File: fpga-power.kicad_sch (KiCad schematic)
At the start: 107 parts, among them U34 XCAU25P-2FFVB676I

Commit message: [#68016] Clean-up the schematic
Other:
- moved on the sheet: R36

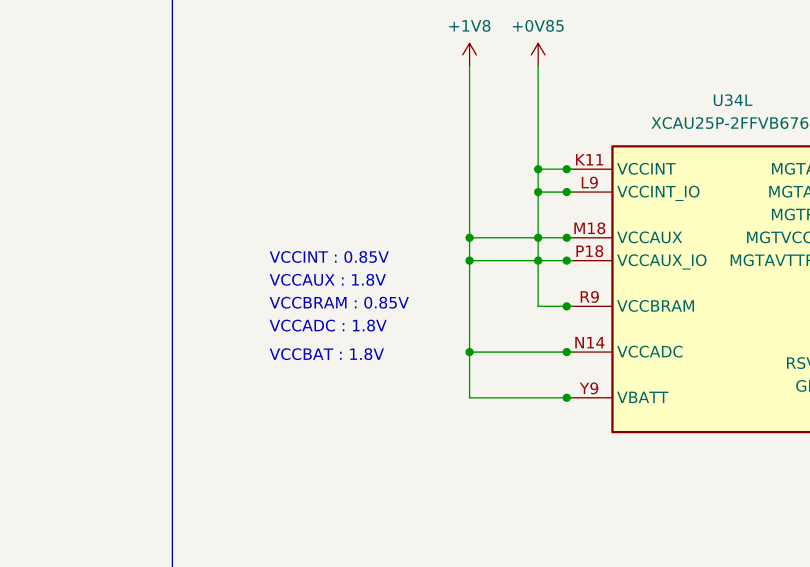
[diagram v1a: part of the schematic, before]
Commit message: [#68016] Fix Power supply short
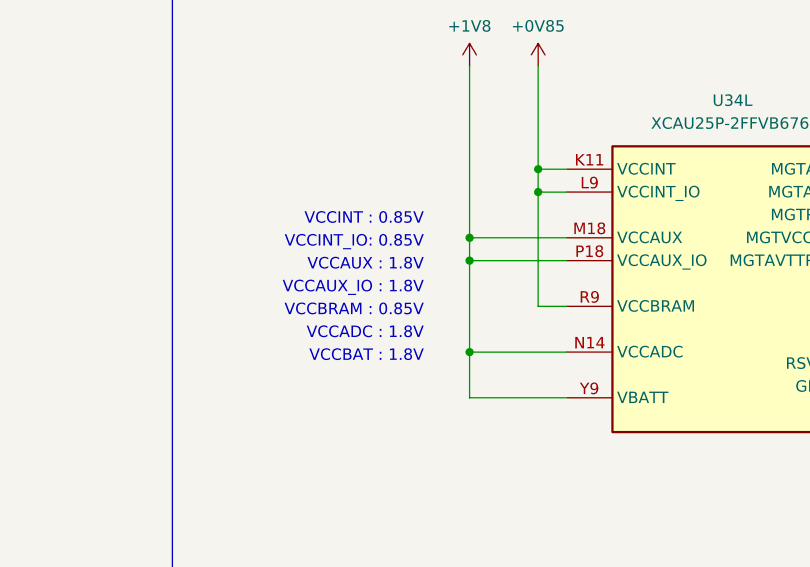
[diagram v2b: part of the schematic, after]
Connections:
- net +0V85: no longer C11.1, C15.2, C18.2, C27.2, C30.2, C68.2, C73.1, C76.2, C77.2, C81.2, C85.1, C87.2, C89.2, C91.2, U34.M18 (VCCAUX), U34.N14 (VCCADC), U34.N18 (VCCAUX), U34.P18 (VCCAUX_IO), U34.R18 (VCCAUX_IO), U34.T18 (VCCAUX_IO), U34.Y9 (VBATT)
- new net +1V8: C11.1, C15.2, C18.2, C27.2, C30.2, C68.2, C73.1, C76.2, C77.2, C81.2, C85.1, C87.2, C89.2, C91.2, U34.M18 (VCCAUX), U34.N14 (VCCADC), U34.N18 (VCCAUX), U34.P18 (VCCAUX_IO), U34.R18 (VCCAUX_IO), U34.T18 (VCCAUX_IO), U34.Y9 (VBATT)
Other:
- note added: "VCCAUX_IO : 1.8V"
- note added: "VCCINT_IO: 0.85V"
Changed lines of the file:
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@@
     (comment 2 "Antmicro Ltd")
   )
-  (junction (at 181.61 121.92) (diameter 0) (color 0 0 0 0)
-  )
   (junction (at 365.76 127) (diameter 0) (color 0 0 0 0)
   )
@@
   (junction (at 356.87 127) (diameter 0) (color 0 0 0 0)
   )
-  (junction (at 184.785 119.38) (diameter 0) (color 0 0 0 0)
-  )
   (junction (at 269.24 114.3) (diameter 0) (color 0 0 0 0)
   )
-  (junction (at 184.785 127) (diameter 0) (color 0 0 0 0)
-  )
   (junction (at 191.77 232.41) (diameter 0) (color 0 0 0 0)
   )
@@
   (junction (at 44.45 163.83) (diameter 0) (color 0 0 0 0)
   )
-  (junction (at 184.785 121.92) (diameter 0) (color 0 0 0 0)
-  )
   (junction (at 53.34 163.83) (diameter 0) (color 0 0 0 0)
   )
@@
   (junction (at 36.83 86.36) (diameter 0) (color 0 0 0 0)
   )
-  (junction (at 184.785 137.16) (diameter 0) (color 0 0 0 0)
-  )
   (junction (at 36.83 110.49) (diameter 0) (color 0 0 0 0)
   )
@@
   (junction (at 95.25 187.96) (diameter 0) (color 0 0 0 0)
   )
-  (junction (at 184.785 132.08) (diameter 0) (color 0 0 0 0)
-  )
   (junction (at 226.06 138.43) (diameter 0) (color 0 0 0 0)
   )
@@
   (junction (at 29.21 232.41) (diameter 0) (color 0 0 0 0)
   )
-  (junction (at 181.61 119.38) (diameter 0) (color 0 0 0 0)
-  )
-  (junction (at 184.785 114.3) (diameter 0) (color 0 0 0 0)
-  )
   (junction (at 80.01 59.69) (diameter 0) (color 0 0 0 0)
   )
@@
   (junction (at 53.34 110.49) (diameter 0) (color 0 0 0 0)
   )
-  (junction (at 184.785 111.76) (diameter 0) (color 0 0 0 0)
-  )
   (wire (pts (xy 44.45 163.83) (xy 53.34 163.83))
     (stroke (width 0) (type default))
@@
     (stroke (width 0) (type default))
   )
-  (wire (pts (xy 184.785 121.92) (xy 185.42 121.92))
-    (stroke (width 0) (type default))
-  )
   (wire (pts (xy 356.87 127) (xy 365.76 127))
     (stroke (width 0) (type default))
@@
     (stroke (width 0) (type default))
   )
-  (wire (pts (xy 181.61 119.38) (xy 184.785 119.38))
-    (stroke (width 0) (type default))
-  )
   (wire (pts (xy 36.83 83.82) (xy 36.83 86.36))
     (stroke (width 0) (type default))
@@
     (stroke (width 0) (type default))
   )
-  (wire (pts (xy 181.61 114.3) (xy 181.61 119.38))
-    (stroke (width 0) (type default))
-  )
   (wire (pts (xy 276.86 231.14) (xy 270.51 231.14))
     (stroke (width 0) (type default))
@@
     (stroke (width 0) (type default))
   )
-  (wire (pts (xy 184.785 127) (xy 185.42 127))
-    (stroke (width 0) (type default))
-  )
   (wire (pts (xy 226.06 135.89) (xy 226.06 138.43))
     (stroke (width 0) (type default))
@@
     (stroke (width 0) (type default))
   )
-  (wire (pts (xy 173.99 121.92) (xy 181.61 121.92))
+  (wire (pts (xy 173.99 121.92) (xy 184.785 121.92))
     (stroke (width 0) (type default))
   )
@@
     (stroke (width 0) (type default))
   )
-  (wire (pts (xy 184.785 137.16) (xy 185.42 137.16))
-    (stroke (width 0) (type default))
-  )
   (wire (pts (xy 340.36 127) (xy 340.36 128.27))
     (stroke (width 0) (type default))
@@
     (stroke (width 0) (type default))
   )
-  (wire (pts (xy 181.61 121.92) (xy 181.61 127))
+  (wire (pts (xy 181.61 114.3) (xy 181.61 127))
     (stroke (width 0) (type default))
   )
@@
     (stroke (width 0) (type default))
   )
-  (wire (pts (xy 181.61 121.92) (xy 184.785 121.92))
-    (stroke (width 0) (type default))
-  )
   (wire (pts (xy 361.95 58.42) (xy 361.95 59.69))
     (stroke (width 0) (type default))
@@
     (stroke (width 0) (type default))
   )
-  (wire (pts (xy 181.61 119.38) (xy 173.99 119.38))
+  (wire (pts (xy 173.99 119.38) (xy 184.785 119.38))
     (stroke (width 0) (type default))
   )
@@
     (stroke (width 0) (type dash))
   )
-  (wire (pts (xy 184.785 111.76) (xy 185.42 111.76))
-    (stroke (width 0) (type default))
-  )
   (wire (pts (xy 36.83 163.83) (xy 44.45 163.83))
     (stroke (width 0) (type default))
@@
     (stroke (width 0) (type default))
   )
-  (wire (pts (xy 184.785 132.08) (xy 185.42 132.08))
-    (stroke (width 0) (type default))
-  )
   (wire (pts (xy 44.45 86.36) (xy 44.45 87.63))
     (stroke (width 0) (type default))
@@
     (stroke (width 0) (type default))
   )
-  (wire (pts (xy 184.785 114.3) (xy 185.42 114.3))
-    (stroke (width 0) (type default))
-  )
   (wire (pts (xy 354.33 93.98) (xy 354.33 95.25))
     (stroke (width 0) (type default))
   )
-  (wire (pts (xy 181.61 119.38) (xy 181.61 121.92))
-    (stroke (width 0) (type default))
-  )
   (wire (pts (xy 45.72 114.3) (xy 45.72 110.49))
     (stroke (width 0) (type default))
@@
     (stroke (width 0) (type default))
   )
-  (wire (pts (xy 184.785 119.38) (xy 185.42 119.38))
-    (stroke (width 0) (type default))
-  )
   (polyline (pts (xy 266.7 264.16) (xy 266.7 271.78))
     (stroke (width 0) (type dash))
@@
     (effects (font (size 1.27 1.27)) (justify left bottom))
   )
-  (text "VCCBAT : 1.8V" (at 151.765 133.35 0)
-    (effects (font (size 1.27 1.27)) (justify left bottom))
+  (text "VCCBAT : 1.8V" (at 168.91 133.35 0)
+    (effects (font (size 1.27 1.27)) (justify right bottom))
   )
   (text "FPGA Power rails" (at 13.335 18.415 0)
@@
     (effects (font (size 1.27 1.27)) (justify left bottom))
   )
-  (text "VCCADC : 1.8V" (at 151.765 130.175 0)
-    (effects (font (size 1.27 1.27)) (justify left bottom))
+  (text "VCCADC : 1.8V" (at 168.91 130.81 0)
+    (effects (font (size 1.27 1.27)) (justify right bottom))
   )
   (text "V_{CCAUX}" (at 40.64 230.505 0)
@@
     (effects (font (size 2 2) (thickness 0.6) bold) (justify left bottom))
   )
-  (text "VCCINT : 0.85V" (at 151.765 122.555 0)
-    (effects (font (size 1.27 1.27)) (justify left bottom))
+  (text "VCCINT_IO: 0.85V" (at 168.91 120.65 0)
+    (effects (font (size 1.27 1.27)) (justify right bottom))
   )
   (text "VCCINT decoupling" (at 16.51 220.98 0)
@@
     (effects (font (size 1.27 1.27)) (justify left bottom))
   )
-  (text "VCCBRAM : 0.85V" (at 151.765 127.635 0)
-    (effects (font (size 1.27 1.27)) (justify left bottom))
+  (text "VCCBRAM : 0.85V" (at 168.91 128.27 0)
+    (effects (font (size 1.27 1.27)) (justify right bottom))
   )
   (text "VCCAVTT : 1.2V" (at 259.08 130.81 0)
@@
     (effects (font (size 2 2) (thickness 0.6) bold) (justify left bottom))
   )
+  (text "VCCINT : 0.85V" (at 168.91 118.11 0)
+    (effects (font (size 1.27 1.27)) (justify right bottom))
+  )
   (text "Bank marked by dashed line \nreferenced from US+ Series FPGAs\nPCB Design Guide UG583\n(AUP25P+ XCKU5P FFVB Package worst case)"
     (at 13.97 27.305 0)
@@
     (effects (font (size 1.27 1.27)) (justify left bottom))
   )
+  (text "VCCAUX_IO : 1.8V" (at 168.91 125.73 0)
+    (effects (font (size 1.27 1.27)) (justify right bottom))
+  )
   (text "BANK 86" (at 236.22 255.27 0)
     (effects (font (size 1.27 1.27)) (justify left bottom))
@@
     (effects (font (size 1.27 1.27)) (justify left bottom))
   )
-  (text "VCCAUX : 1.8V" (at 151.765 125.095 0)
-    (effects (font (size 1.27 1.27)) (justify left bottom))
+  (text "VCCAUX : 1.8V" (at 168.91 123.19 0)
+    (effects (font (size 1.27 1.27)) (justify right bottom))
   )
   (text "VCCINT decoupling" (at 13.97 44.45 0)

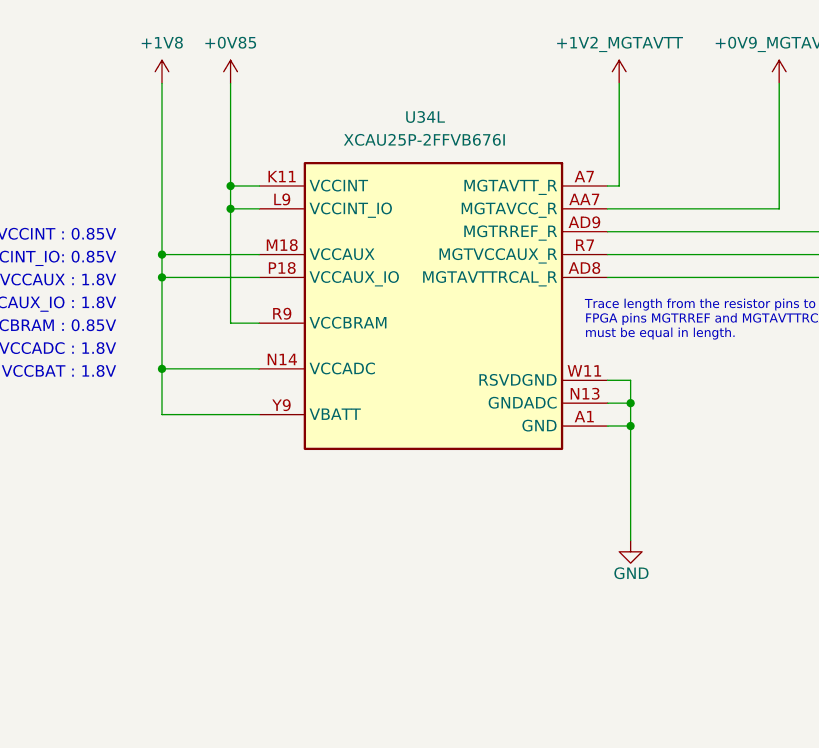
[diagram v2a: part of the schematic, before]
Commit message: [#68016] Solve ERC warrings and errors
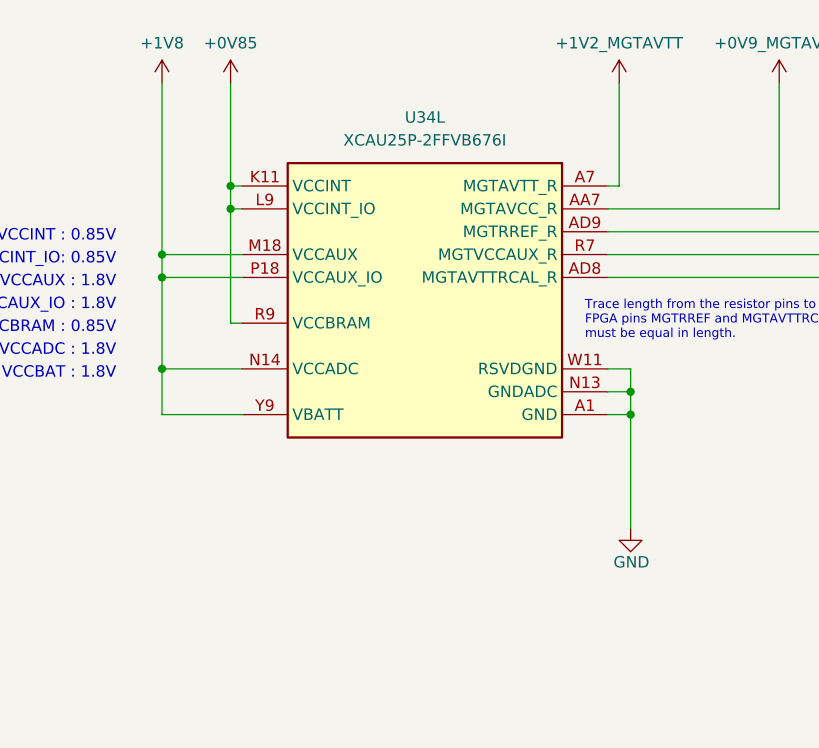
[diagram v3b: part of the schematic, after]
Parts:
- C100, C101, C102, C103, C104, C105, C106, C107, C108, C13, C15, C16, C167, C168, C17, C18, C19, C20, C23, C24, C243, C246, C247, C248, C26, C27, C30, C310, C311, C312, C33, C34, C35, C36, C37, C39, C40, C41, C42, C43, C45, C46, C47, C48, C49, C50, C51, C52, C53, C55, C56, C57, C58, C59, C60, C61, C64, C65, C67, C68, C70, C71, C72, C74, C75, C76, C77, C78, C79, C80, C81, C83, C84, C86, C87, C88, C89, C90, C91, C92, C95, C96, C97, C98, C99: footprint antmicro-footprints:C_0402_1005Metric_EIA -> antmicro-footprints:C_0402_1005Metric
- R36: footprint antmicro-footprints:R_0402_1005Metric_EIA -> antmicro-footprints:R_0402_1005Metric
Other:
- moved on the sheet: U34L

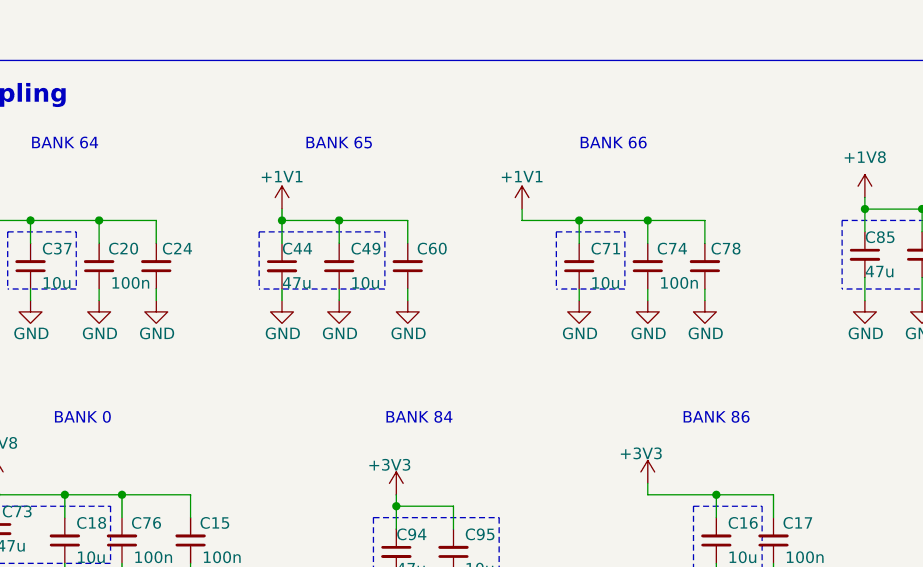
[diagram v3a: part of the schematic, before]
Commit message: [#68199] Start implementing changes after the PCB review
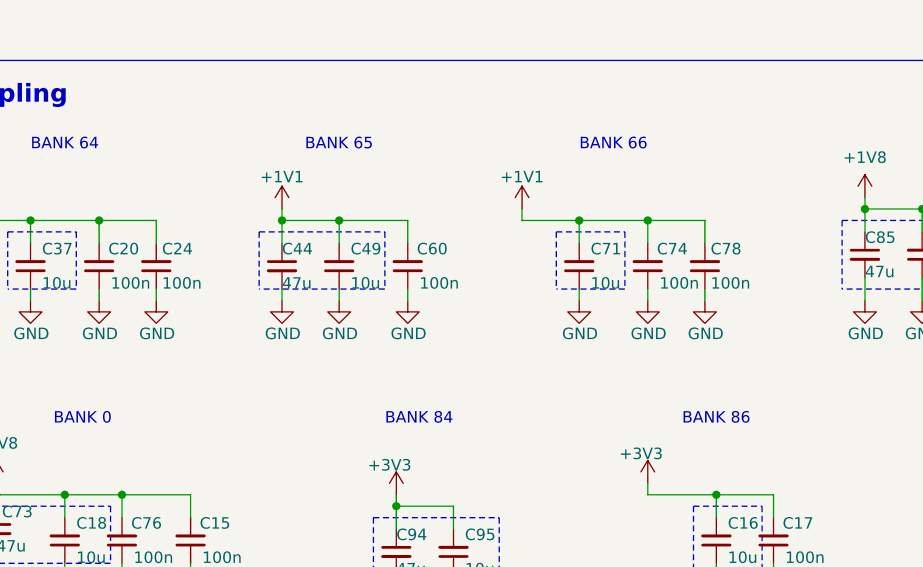
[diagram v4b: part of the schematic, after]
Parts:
- C100, C101, C102, C103, C104, C105, C106, C107, C108, C13, C15, C16, C167, C168, C17, C18, C19, C20, C23, C24, C243, C246, C247, C248, C26, C27, C30, C310, C311, C312, C33, C34, C35, C36, C37, C39, C40, C41, C42, C43, C45, C46, C47, C48, C49, C50, C51, C52, C53, C55, C56, C57, C58, C59, C60, C61, C64, C65, C67, C68, C70, C71, C72, C74, C75, C76, C77, C78, C79, C80, C81, C83, C84, C86, C87, C88, C89, C90, C91, C92, C95, C96, C97, C98, C99: footprint antmicro-footprints:C_0402_1005Metric -> antmicro-footprints:C_0402_1005Metric_EIA
- R36: footprint antmicro-footprints:R_0402_1005Metric -> antmicro-footprints:R_0402_1005Metric_EIA
